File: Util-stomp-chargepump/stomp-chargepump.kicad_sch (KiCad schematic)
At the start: 12 parts, among them J1 1x8, U1 MAX1044

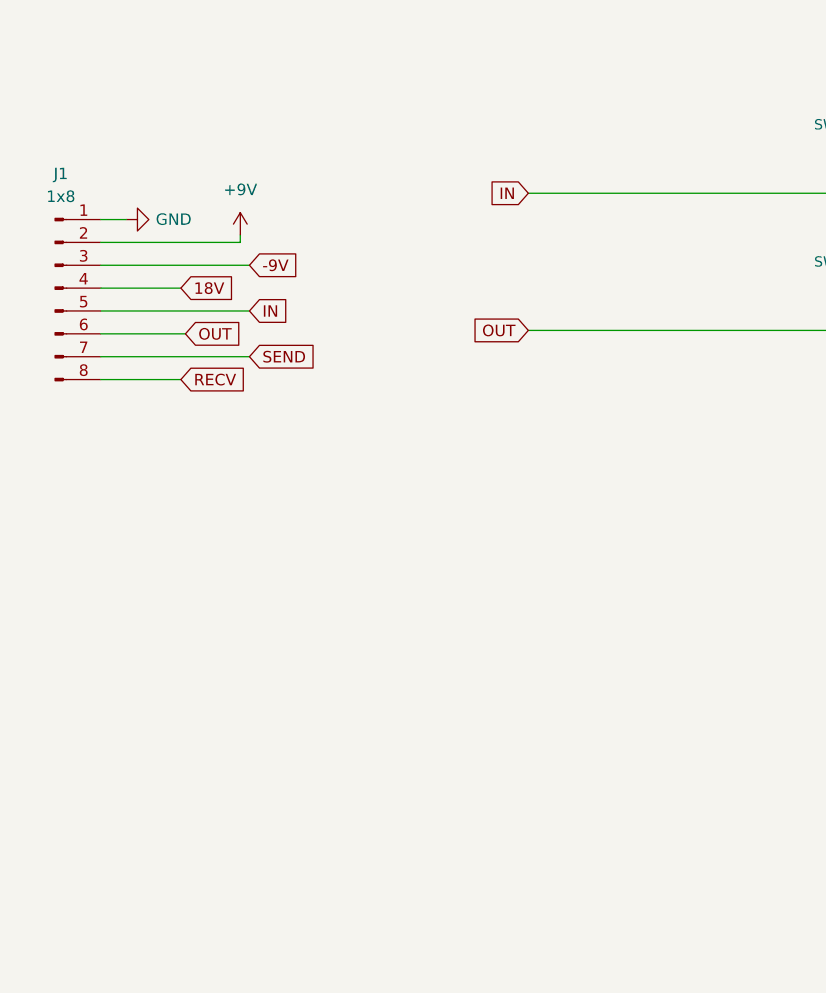
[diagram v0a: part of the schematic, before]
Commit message: added tweed57 overdrive
updated layout of the chargepump pcb
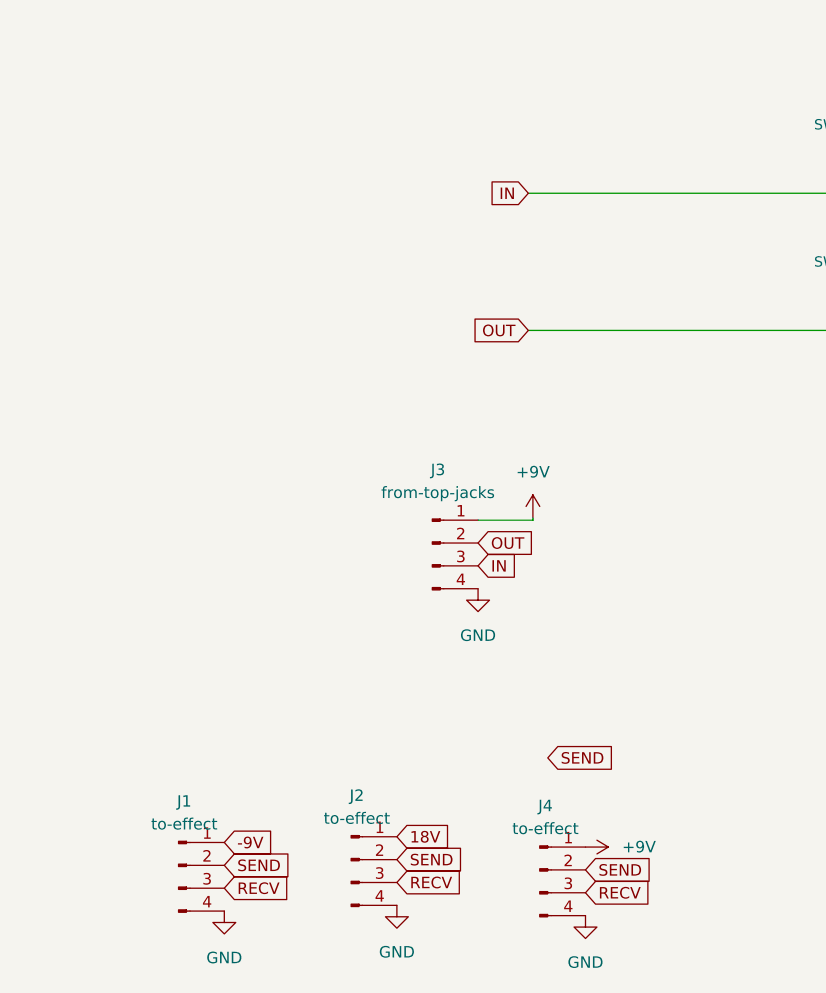
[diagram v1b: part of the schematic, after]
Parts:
- removed J1: 1x8, Connector_PinHeader_2.54mm:PinHeader_1x08_P2.54mm_Vertical, symbol Connector:Conn_01x08_Male
- added J1, J2, J4: to-effect, Connector_PinHeader_2.54mm:PinHeader_1x04_P2.54mm_Vertical, symbol Connector:Conn_01x04_Pin
- added J3: from-top-jacks, Connector_PinHeader_2.54mm:PinHeader_1x04_P2.54mm_Vertical, symbol Connector:Conn_01x04_Pin
- U1: footprint (none) -> Package_DIP:DIP-8_W7.62mm_LongPads
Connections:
- net +9V: now also J3.1 (Pin_1), J4.1 (Pin_1)
- net -9V: now also J1.1 (Pin_1)
- net 18V: now also J2.1 (Pin_1)
- net GND: now also J1.4 (Pin_4), J2.4 (Pin_4), J3.4 (Pin_4), J4.4 (Pin_4)
- net IN: now also J3.3 (Pin_3)
- net OUT: now also J3.2 (Pin_2)
- net RECV: now also J1.3 (Pin_3), J2.3 (Pin_3), J4.3 (Pin_3)
- net SEND: now also J1.2 (Pin_2), J2.2 (Pin_2), J4.2 (Pin_2)
